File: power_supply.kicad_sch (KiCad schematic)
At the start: 42 parts

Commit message: Schematic updated
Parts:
- removed U?: NCV8164ASN330T1G, Package_TO_SOT_SMD:SOT-23-5, symbol Regulator_Linear:AP2204K-1.5
- removed U?: NCV8164ASN120T1G, Package_TO_SOT_SMD:SOT-23-5, symbol Regulator_Linear:AP2204K-1.5
- removed U?: NCV8164ASN250T1G, Package_TO_SOT_SMD:SOT-23-5, symbol Regulator_Linear:AP2204K-1.5
- added D908, D909, D910, D911: D_Zener, symbol Device:D_Zener
- added R905, R906: 10k, Resistor_SMD:R_0805_2012Metric, symbol Device:R
- added U902: NCV8164ASN120T1G, Package_TO_SOT_SMD:SOT-23-5, symbol symbols:NCV8164
- added U904: NCV8164ASN250T1G, Package_TO_SOT_SMD:SOT-23-5, symbol symbols:NCV8164
- added U905: NCV8164ASN330T1G, Package_TO_SOT_SMD:SOT-23-5, symbol symbols:NCV8164
- C901, C902, C903, C904, C905, C906, C908, C909, C910, C911, C912, C913: renamed from C?; footprint (none) -> Capacitor_SMD:C_0805_2012Metric
- R901, R902, R903, R904: renamed from R?; footprint (none) -> Resistor_SMD:R_0805_2012Metric
- TP901, TP902, TP903, TP904, TP905, TP906, TP907, TP908: renamed from TP?; footprint (none) -> TestPoint:TestPoint_THTPad_D1.0mm_Drill0.5mm
- gave numbers to parts that had none: 15
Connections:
- net GND: now also D908.2 (A), D909.2 (A), D910.2 (A), D911.2 (A), U902.2 (GND), U904.2 (GND), U905.2 (GND)
- net OUT_1V2D: now also TP904.1, D908.1 (K), U902.5 (Vout); no longer TP905.1
- net OUT_2V5A: now also D910.1 (K), U904.5 (Vout)
- net OUT_3V3A: now also D911.1 (K), U905.5 (Vout)
- net OUT_3V3D: now also TP905.1, D909.1 (K); no longer TP904.1
- net OUT_3V3_FT: now also Q901.1 (G)
- net OUT_5VMAIN: now also R905.2, R906.2, U902.1 (Vin), U904.1 (Vin), U905.1 (Vin)
- net at R903.1, U901.5 (PWRGD): now also U902.3 (EN); no longer U903.1 (~{SHDN})
- net at U903.5 (PWRGD): now also R905.1, U904.3 (EN); no longer R904.1
- new net: R906.1, U904.4 (PWRGD), U905.3 (EN)
- new net: R904.1, U902.4 (PWRGD), U903.1 (~{SHDN})
- new net PGOOD: U905.4 (PWRGD)
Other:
- note added: "LDO turn on sequencing: 1. FTDI 3V3 rail 2. 1V2D rail (iCE40 VCC) 3. Main 3V3D rail 4. 2V5A rail (ADC VDD) 5. 3V3A rail (input amps & osc)"
- note removed: "LDO turn on sequencing: 1. FTDI 3V3 rail 2. Main 3V3D rail 3. All other rails"
- moved on the sheet: C910, C911, C912, C913, R903, R904, TP903, TP904, TP905, TP906, TP907, U903

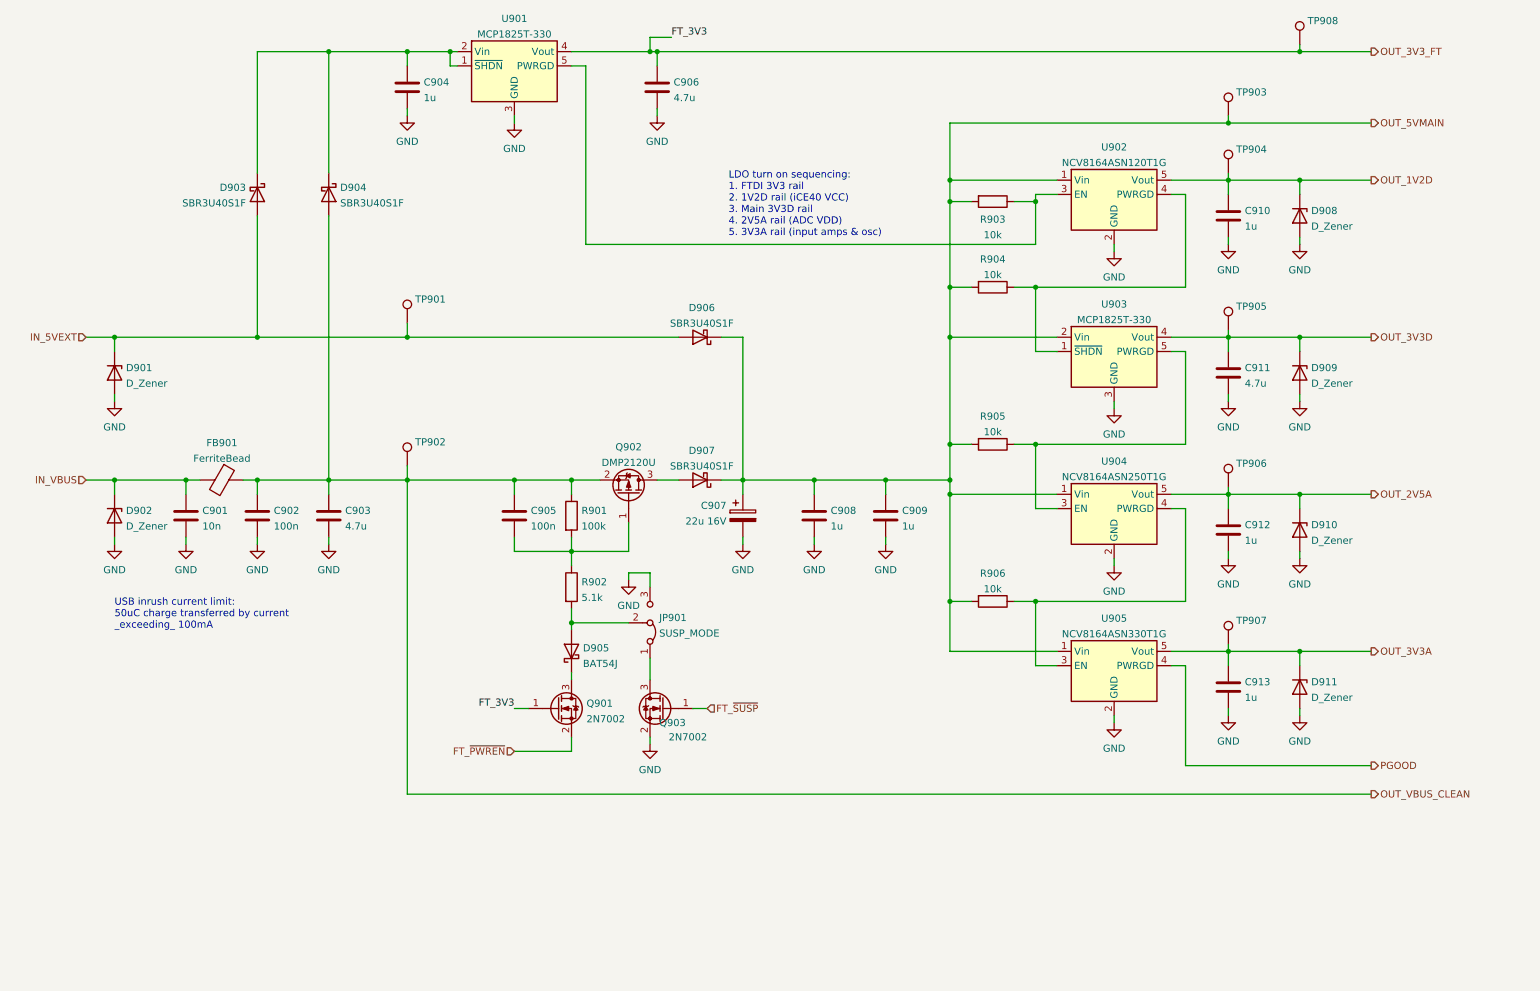
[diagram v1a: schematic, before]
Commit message: Schematic sketching done
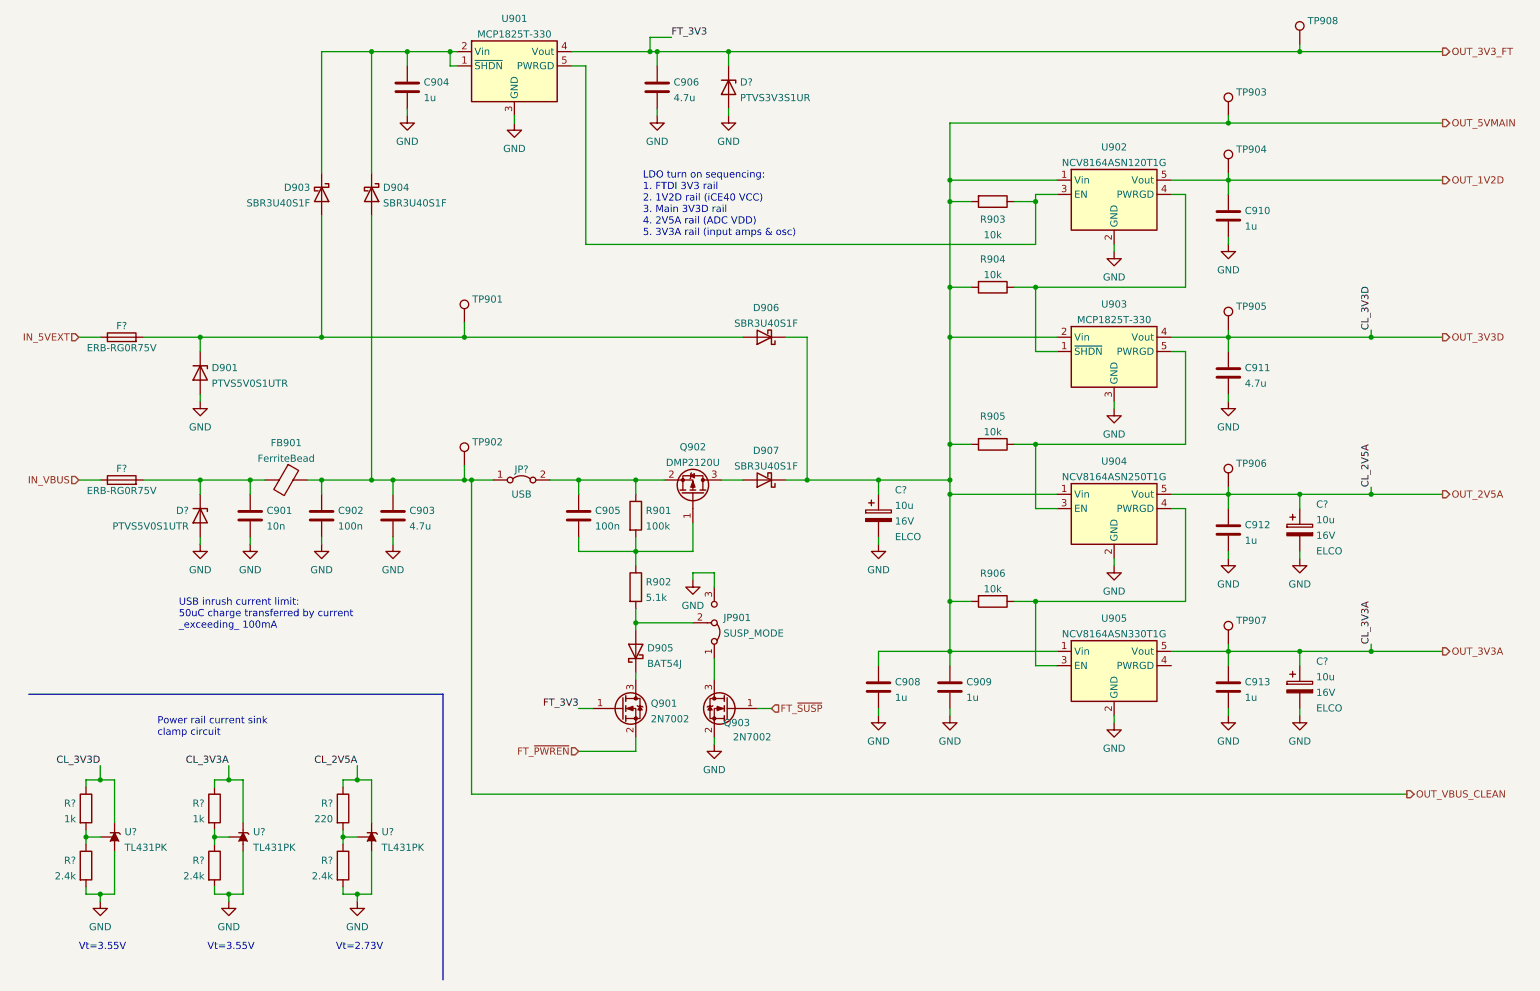
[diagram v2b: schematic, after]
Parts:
- removed C907: 22u 16V, symbol Device:C_Polarized
- removed D902, D908, D909, D910, D911: D_Zener, symbol Device:D_Zener
- added C? (x3): 10u, symbol Device:C_Polarized
- added D?: PTVS3V3S1UR, symbol Device:D_Zener
- added D?: PTVS5V0S1UTR, symbol Device:D_Zener
- added F? (x2): ERB-RG0R75V, symbol Device:Fuse
- added JP?: USB, symbol Jumper:Jumper_2_Bridged
- added R? (x3): 2.4k, Resistor_SMD:R_0805_2012Metric, symbol Device:R
- added R?: 220, Resistor_SMD:R_0805_2012Metric, symbol Device:R
- added R? (x2): 1k, Resistor_SMD:R_0805_2012Metric, symbol Device:R
- added U? (x3): TL431PK, Package_TO_SOT_SMD:SOT-89-3, symbol Reference_Voltage:TL431PK
- D901: value D_Zener -> PTVS5V0S1UTR
- R901, R902, R903, R904, R905, R906: Tolerance (none) -> 5%
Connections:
- net GND: now also C?.2, C?.2, C?.2, D?.2 (A), D?.2 (A), R?.2, R?.2, R?.2, U?.2 (A), U?.2 (A), U?.2 (A)
- net IN_5VEXT: now also F?.1; no longer D901.1 (K), D903.2 (A), D906.2 (A), TP901.1
- net IN_VBUS: now also F?.1; no longer C901.1, FB901.2
- net OUT_2V5A: now also C?.1, R?.1, U?.3 (K)
- net OUT_3V3A: now also C?.1, R?.1, U?.3 (K)
- net OUT_3V3D: now also R?.1, U?.3 (K)
- net OUT_3V3_FT: now also D?.1 (K)
- net OUT_5VMAIN: now also C?.1
- net OUT_VBUS_CLEAN: now also JP?.1 (A); no longer C905.1, Q902.2 (S), R901.1
- net PGOOD: no longer names the net of U905.4 (PWRGD)
- new net: R?.1, R?.2, U?.1 (REF) (x3)
- new net: D901.1 (K), D903.2 (A), D906.2 (A), F?.2, TP901.1
- new net: C905.1, JP?.2 (B), Q902.2 (S), R901.1
- new net: C901.1, D?.1 (K), F?.2, FB901.2
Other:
- note added: "Power rail current sink clamp circuit"
- note added: "Vt=2.73V"
- note added: "Vt=3.55V"
- moved on the sheet: C901, C902, C903, C905, C908, C909, D901, D903, D904, D905, D906, D907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

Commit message: Update schematic layout, separate into sheets
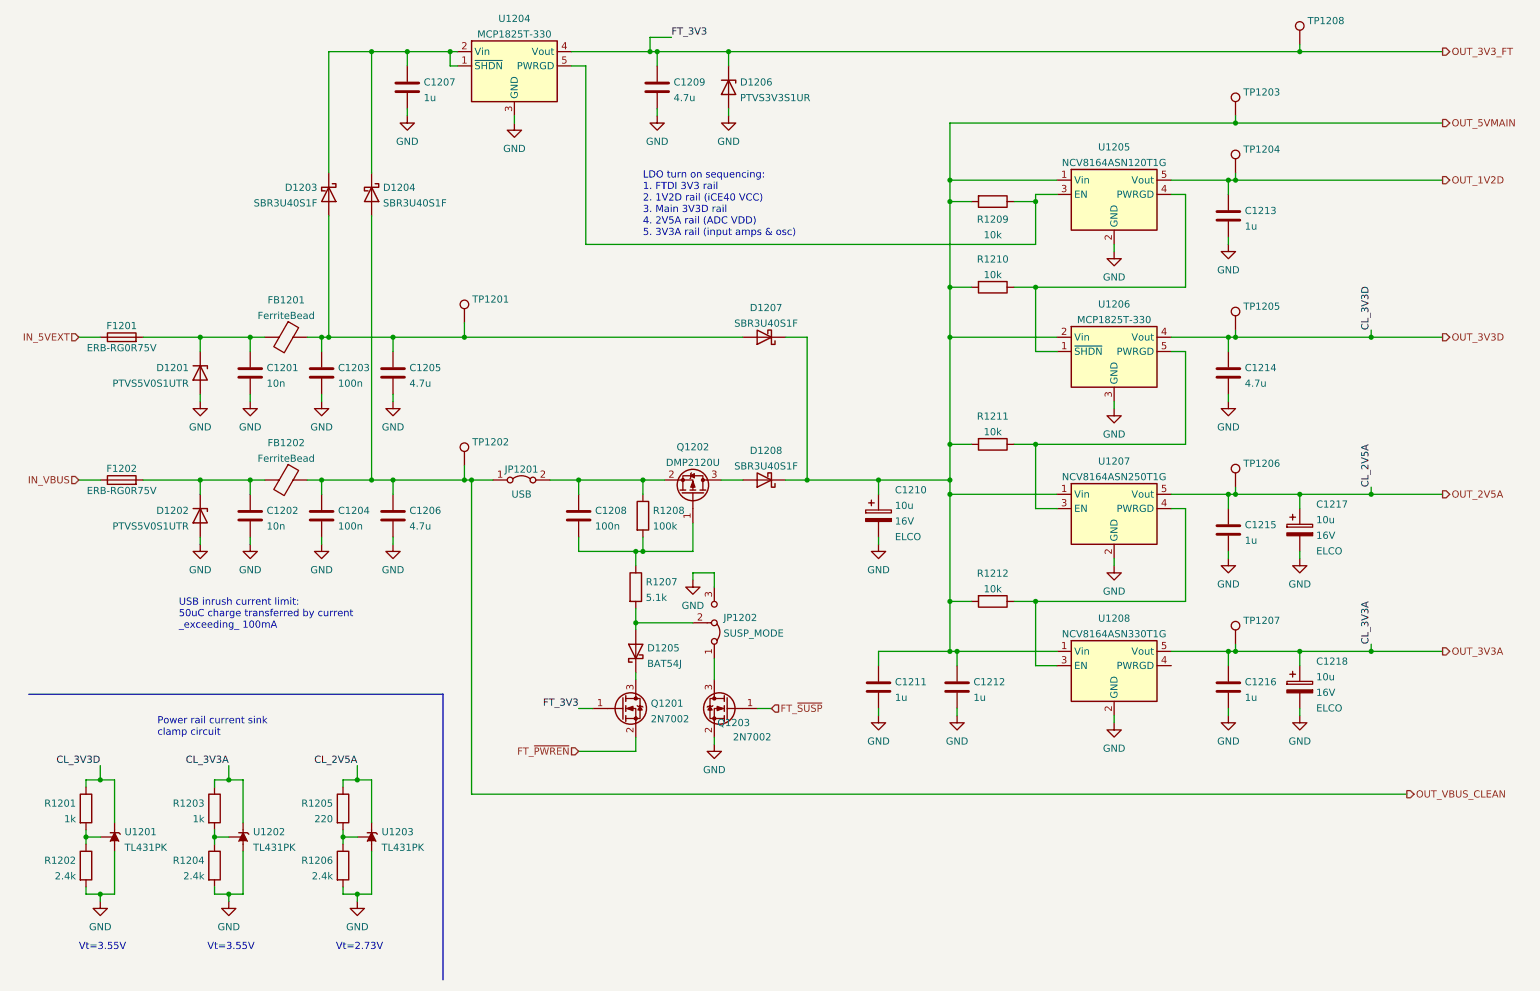
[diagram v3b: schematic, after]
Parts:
- added C1201: 10n, Capacitor_SMD:C_0805_2012Metric, symbol Device:C
- added C1203: 100n, Capacitor_SMD:C_0805_2012Metric, symbol Device:C
- added C1205: 4.7u, Capacitor_SMD:C_0805_2012Metric, symbol Device:C
- added FB1201: FerriteBead, symbol Device:FerriteBead
- gave numbers to parts that had none: 17
- renumbered C901 to C1202, C902 to C1204, C903 to C1206, C904 to C1207, C905 to C1208, C906 to C1209, C908 to C1211, C909 to C1212, C910 to C1213, C911 to C1214, C912 to C1215, C913 to C1216, D901 to D1201, D903 to D1203, D904 to D1204, D905 to D1205, D906 to D1207, D907 to D1208, FB901 to FB1202, JP901 to JP1202, Q901 to Q1201, Q902 to Q1202, Q903 to Q1203, R902 to R1207, R901 to R1208, R903 to R1209, R904 to R1210, R905 to R1211, R906 to R1212, TP901 to TP1201, TP902 to TP1202, TP903 to TP1203, TP904 to TP1204, TP905 to TP1205, TP906 to TP1206, TP907 to TP1207, TP908 to TP1208, U901 to U1204, U902 to U1205, U903 to U1206, U904 to U1207, U905 to U1208
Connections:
- net GND: now also C1201.2, C1203.2, C1205.2
- net at D1203.2 (A), D1207.2 (A), TP1201.1: now also C1203.1, C1205.1, FB1201.1; no longer D1201.1 (K), F1201.2
- new net: C1201.1, D1201.1 (K), F1201.2, FB1201.2
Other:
- moved on the sheet: C1212, D1203, R1208, TP1203, TP1204, TP1205, TP1206, TP1207

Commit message: Schematic update
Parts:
- removed JP1202: SUSP_MODE, symbol Jumper:Jumper_3_Bridged12
- removed Q1203: 2N7002, Package_TO_SOT_SMD:SOT-23, symbol Transistor_FET:2N7002
- added JP1202: USB_PON, Connector_PinHeader_2.54mm:PinHeader_1x02_P2.54mm_Vertical, symbol Jumper:Jumper_2_Open
- C1201, C1202: value 10n -> 100n; Spec1 (none) -> 16V; Spec2 (none) -> X5R; Tolerance (none) -> 20%
- C1203, C1204, C1205, C1206, C1207, C1208, C1209, C1211, C1212, C1214, C1215, C1216: Spec1 (none) -> 16V; Spec2 (none) -> X5R; Tolerance (none) -> 20%
- C1210, C1217, C1218: footprint (none) -> Capacitor_SMD:CP_Elec_4x5.8; Tolerance (none) -> 20%
- C1213: value 1u -> 4.7u; Spec1 (none) -> 16V; Spec2 (none) -> X5R; Tolerance (none) -> 20%
- F1201, F1202: value ERB-RG0R75V -> 1206L050/15; footprint (none) -> Fuse:Fuse_1206_3216Metric
- JP1201: footprint (none) -> Connector_PinHeader_2.54mm:PinHeader_1x02_P2.54mm_Vertical
- Q1202: footprint (none) -> Package_TO_SOT_SMD:SOT-23
- renumbered TP1208 to TP1203, TP1203 to TP1204, TP1204 to TP1205, TP1205 to TP1206, TP1206 to TP1207, TP1207 to TP1208
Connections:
- net GND: now also JP1202.2 (B)
- net at D1205.2 (A), R1207.2: now also JP1202.1 (A)
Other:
- moved on the sheet: TP1203
